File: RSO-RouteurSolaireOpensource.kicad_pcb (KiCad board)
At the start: 2 copper layers, 100 x 105 mm, 40 parts

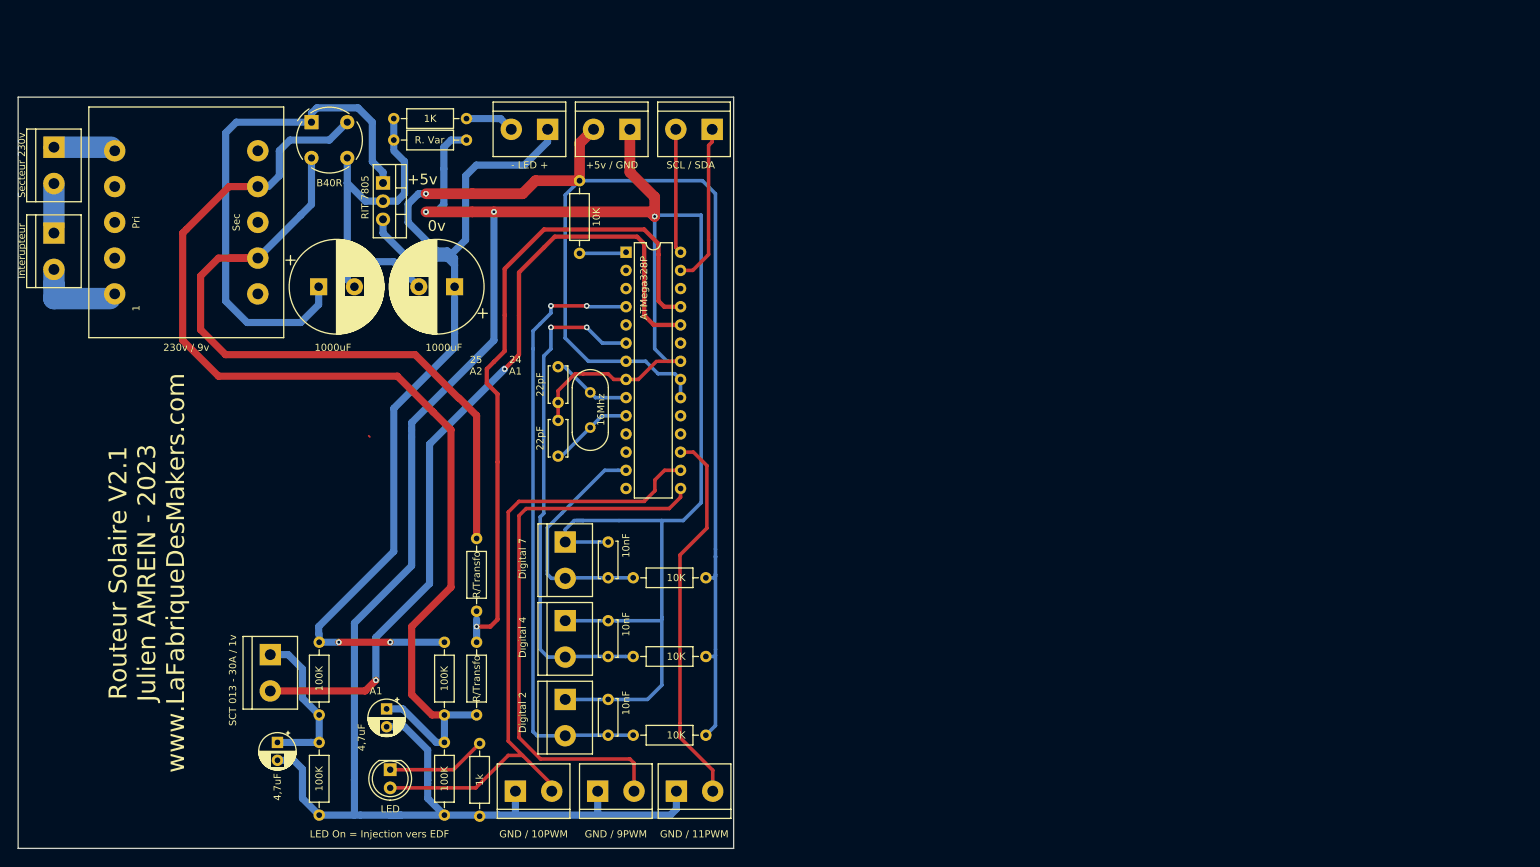
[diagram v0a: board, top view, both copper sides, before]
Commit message: MAJ Sur carte sct013
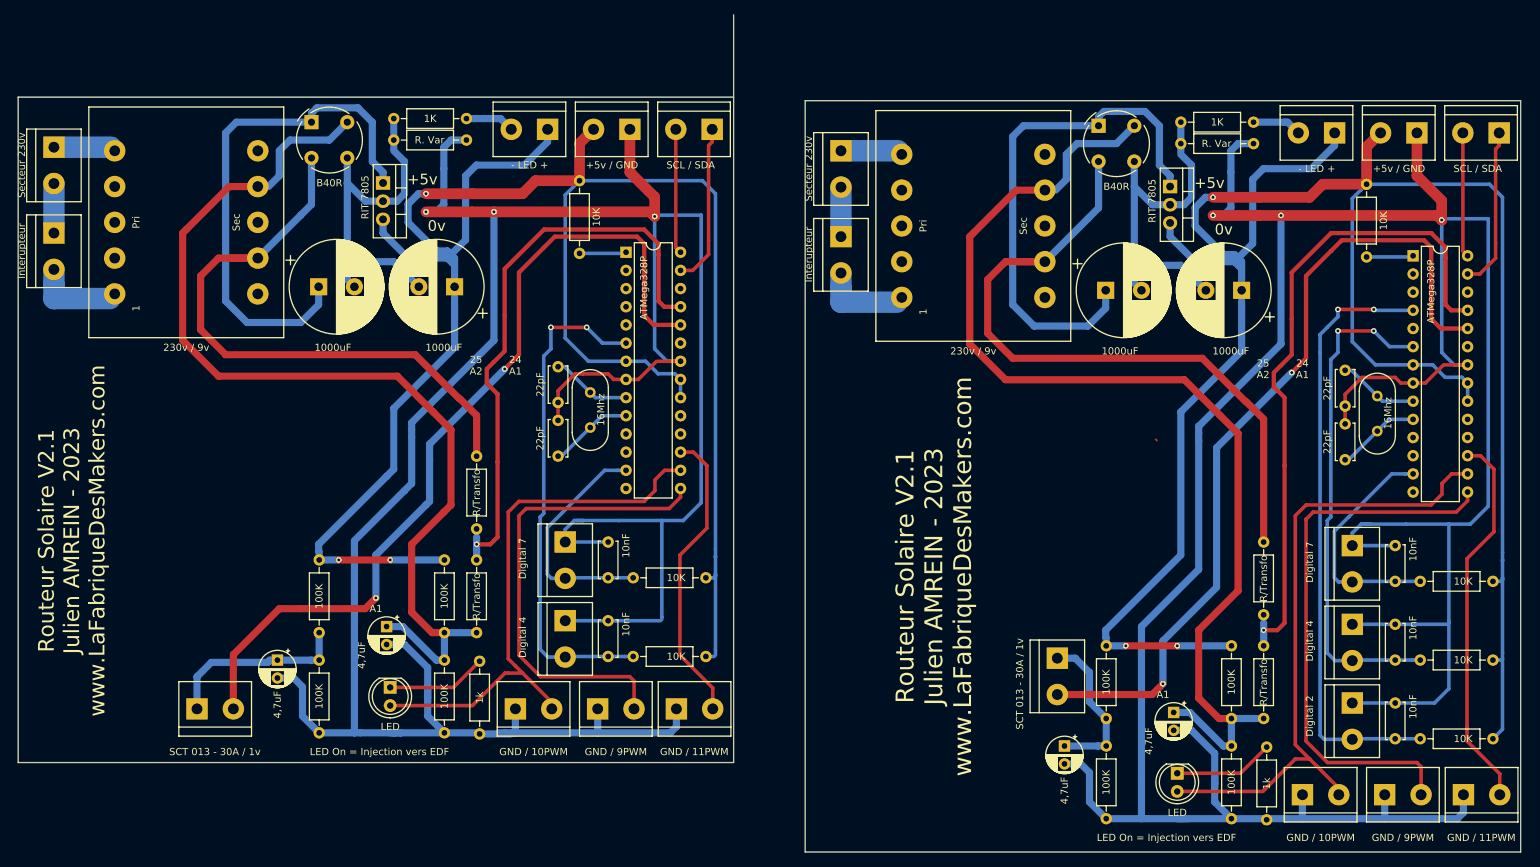
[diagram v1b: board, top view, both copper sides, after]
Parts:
- removed the 10K at (121.0, 143.7)
- removed the 10nF at (117.5, 138.7)
- removed the R/Transfo at (99.1, 116.2)
- removed the R/Transfo at (99.1, 130.7)
- removed the SCT 013 - 30A / 1v at (70.2, 132.4)
- added +5v / GND: TerminalBlock_bornier-2_P5.08mm, TerminalBlock:TerminalBlock_bornier-2_P5.08mm, F.Cu at (230.5, 59.5)
- added - LED +: TerminalBlock_bornier-2_P5.08mm, TerminalBlock:TerminalBlock_bornier-2_P5.08mm, F.Cu at (219.0, 59.5)
- added 1000uF: CP_Radial_D13.0mm_P5.00mm, Capacitor_THT:CP_Radial_D13.0mm_P5.00mm, F.Cu at (206.0, 81.5)
- added 1000uF: CP_Radial_D13.0mm_P5.00mm, Capacitor_THT:CP_Radial_D13.0mm_P5.00mm, F.Cu at (187.0, 81.5)
- added 100K: R_Axial_DIN0207_L6.3mm_D2.5mm_P10.16mm_Horizontal, Resistor_THT:R_Axial_DIN0207_L6.3mm_D2.5mm_P10.16mm_Horizontal, F.Cu at (204.6, 131.2)
- added 100K: R_Axial_DIN0207_L6.3mm_D2.5mm_P10.16mm_Horizontal, Resistor_THT:R_Axial_DIN0207_L6.3mm_D2.5mm_P10.16mm_Horizontal, F.Cu at (204.6, 145.2)
- added 100K: R_Axial_DIN0207_L6.3mm_D2.5mm_P10.16mm_Horizontal, Resistor_THT:R_Axial_DIN0207_L6.3mm_D2.5mm_P10.16mm_Horizontal, F.Cu at (187.1, 131.2)
- added 100K: R_Axial_DIN0207_L6.3mm_D2.5mm_P10.16mm_Horizontal, Resistor_THT:R_Axial_DIN0207_L6.3mm_D2.5mm_P10.16mm_Horizontal, F.Cu at (187.1, 145.2)
- added 10K: R_Axial_DIN0207_L6.3mm_D2.5mm_P10.16mm_Horizontal, Resistor_THT:R_Axial_DIN0207_L6.3mm_D2.5mm_P10.16mm_Horizontal, F.Cu at (223.5, 66.7)
- added 10K: R_Axial_DIN0207_L6.3mm_D2.5mm_P10.16mm_Horizontal, Resistor_THT:R_Axial_DIN0207_L6.3mm_D2.5mm_P10.16mm_Horizontal, F.Cu at (231.0, 133.2)
- added 10K: R_Axial_DIN0207_L6.3mm_D2.5mm_P10.16mm_Horizontal, Resistor_THT:R_Axial_DIN0207_L6.3mm_D2.5mm_P10.16mm_Horizontal, F.Cu at (231.0, 122.2)
- added 10K: R_Axial_DIN0207_L6.3mm_D2.5mm_P10.16mm_Horizontal, Resistor_THT:R_Axial_DIN0207_L6.3mm_D2.5mm_P10.16mm_Horizontal, F.Cu at (231.0, 144.2)
- added 10nF: C_Disc_D5.0mm_W2.5mm_P5.00mm, Capacitor_THT:C_Disc_D5.0mm_W2.5mm_P5.00mm, F.Cu at (227.5, 117.2)
- added 10nF: C_Disc_D5.0mm_W2.5mm_P5.00mm, Capacitor_THT:C_Disc_D5.0mm_W2.5mm_P5.00mm, F.Cu at (227.5, 128.2)
- added 10nF: C_Disc_D5.0mm_W2.5mm_P5.00mm, Capacitor_THT:C_Disc_D5.0mm_W2.5mm_P5.00mm, F.Cu at (227.5, 139.2)
- added 16Mhz: Crystal_HC18-U_Vertical, Crystal:Crystal_HC18-U_Vertical, F.Cu at (225.0, 101.2)
- added 1K: R_Axial_DIN0207_L6.3mm_D2.5mm_P10.16mm_Horizontal, Resistor_THT:R_Axial_DIN0207_L6.3mm_D2.5mm_P10.16mm_Horizontal, F.Cu at (197.5, 58.0)
- added 1k: R_Axial_DIN0207_L6.3mm_D2.5mm_P10.16mm_Horizontal, Resistor_THT:R_Axial_DIN0207_L6.3mm_D2.5mm_P10.16mm_Horizontal, F.Cu at (209.5, 155.5)
- added 22pF: C_Disc_D5.0mm_W2.5mm_P5.00mm, Capacitor_THT:C_Disc_D5.0mm_W2.5mm_P5.00mm, F.Cu at (220.5, 92.7)
- added 22pF: C_Disc_D5.0mm_W2.5mm_P5.00mm, Capacitor_THT:C_Disc_D5.0mm_W2.5mm_P5.00mm, F.Cu at (220.5, 100.2)
- added 230v / 9v: 230v - 5v AC, Transformer_THT:Transformer_CHK_EI30-2VA_1xSec, F.Cu at (158.5, 82.5)
- added 4,7uF: CP_Radial_D5.0mm_P2.50mm, Capacitor_THT:CP_Radial_D5.0mm_P2.50mm, F.Cu at (196.5, 140.5)
- added 4,7uF: CP_Radial_D5.0mm_P2.50mm, Capacitor_THT:CP_Radial_D5.0mm_P2.50mm, F.Cu at (181.2, 145.2)
- added ATMega328P: DIP-28_W7.62mm, Package_DIP:DIP-28_W7.62mm, F.Cu at (230.0, 76.7)
- added B40R: Diode_Bridge_Round_D9.0mm, Diode_THT:Diode_Bridge_Round_D9.0mm, F.Cu at (186.0, 58.5)
- added Digital 4: TerminalBlock_bornier-2_P5.08mm, TerminalBlock:TerminalBlock_bornier-2_P5.08mm, F.Cu at (221.5, 128.2)
- added Digital 7: TerminalBlock_bornier-2_P5.08mm, TerminalBlock:TerminalBlock_bornier-2_P5.08mm, F.Cu at (221.5, 117.2)
- added GND / 10PWM: TerminalBlock_bornier-2_P5.08mm, TerminalBlock:TerminalBlock_bornier-2_P5.08mm, F.Cu at (214.5, 152.0)
- added GND / 11PWM: TerminalBlock_bornier-2_P5.08mm, TerminalBlock:TerminalBlock_bornier-2_P5.08mm, F.Cu at (237.0, 152.0)
- added GND / 9PWM: TerminalBlock_bornier-2_P5.08mm, TerminalBlock:TerminalBlock_bornier-2_P5.08mm, F.Cu at (226.0, 152.0)
- added Interupteur: TerminalBlock_bornier-2_P5.08mm, TerminalBlock:TerminalBlock_bornier-2_P5.08mm, F.Cu at (150.0, 74.0)
- added LED: LED_D5.0mm, LED_THT:LED_D5.0mm, F.Cu at (197.0, 149.0)
- added R. Var: R_Axial_DIN0207_L6.3mm_D2.5mm_P10.16mm_Horizontal, Resistor_THT:R_Axial_DIN0207_L6.3mm_D2.5mm_P10.16mm_Horizontal, F.Cu at (197.5, 61.0)
- added R/Transfo: R_Axial_DIN0207_L6.3mm_D2.5mm_P10.16mm_Horizontal, Resistor_THT:R_Axial_DIN0207_L6.3mm_D2.5mm_P10.16mm_Horizontal, F.Cu at (209.1, 131.2)
- added R/Transfo: R_Axial_DIN0207_L6.3mm_D2.5mm_P10.16mm_Horizontal, Resistor_THT:R_Axial_DIN0207_L6.3mm_D2.5mm_P10.16mm_Horizontal, F.Cu at (209.1, 116.7)
- added R/Transfo: R_Axial_DIN0207_L6.3mm_D2.5mm_P10.16mm_Horizontal, Resistor_THT:R_Axial_DIN0207_L6.3mm_D2.5mm_P10.16mm_Horizontal, F.Cu at (99.1, 104.7)
- added R/Transfo: R_Axial_DIN0207_L6.3mm_D2.5mm_P10.16mm_Horizontal, Resistor_THT:R_Axial_DIN0207_L6.3mm_D2.5mm_P10.16mm_Horizontal, F.Cu at (99.1, 119.2)
- added RIT 7805: TO-220-3_Vertical, Package_TO_SOT_THT:TO-220-3_Vertical, F.Cu at (196.0, 67.0)
- added SCL / SDA: TerminalBlock_bornier-2_P5.08mm, TerminalBlock:TerminalBlock_bornier-2_P5.08mm, F.Cu at (242.0, 59.5)
- added SCT 013 - 30A / 1v: TerminalBlock_bornier-2_P5.08mm, TerminalBlock:TerminalBlock_bornier-2_P5.08mm, F.Cu at (60.0, 140.0)
- added SCT 013 - 30A / 1v: TerminalBlock_bornier-2_P5.08mm, TerminalBlock:TerminalBlock_bornier-2_P5.08mm, F.Cu at (180.2, 132.9)
- added Secteur 230v : TerminalBlock_bornier-2_P5.08mm, TerminalBlock:TerminalBlock_bornier-2_P5.08mm, F.Cu at (150.0, 62.0)
- moved Digital 2 110.0 mm to (221.5, 139.2)
- moved 100K 11.5 mm to (94.6, 119.2)
- moved 100K 11.5 mm to (77.1, 119.2)
- moved 100K 11.5 mm to (94.6, 133.2)
- moved 100K 11.5 mm to (77.1, 133.2)
- moved 1k 11.5 mm to (99.5, 143.5)
- moved 4,7uF 11.5 mm to (86.5, 128.5)
- moved 4,7uF 11.5 mm to (71.2, 133.2)
- moved GND / 10PWM 11.5 mm to (104.5, 140.0)
- moved GND / 11PWM 11.5 mm to (127.0, 140.0)
- moved GND / 9PWM 11.5 mm to (116.0, 140.0)
- moved LED 11.5 mm to (87.0, 137.0)
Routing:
- net (no net): track 1866.9 -> 3531.5 mm, vias 13 -> 24
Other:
- board size 100 x 105 mm -> 210 x 117 mm

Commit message: Gerber inclus
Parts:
- removed the +5v / GND at (230.5, 59.5)
- removed the - LED + at (219.0, 59.5)
- removed the 1000uF at (206.0, 81.5)
- removed the 1000uF at (187.0, 81.5)
- removed the 100K at (204.6, 131.2)
- removed the 100K at (204.6, 145.2)
- removed the 100K at (187.1, 131.2)
- removed the 100K at (187.1, 145.2)
- removed the 10K at (223.5, 66.7)
- removed the 10K at (231.0, 133.2)
- removed the 10K at (231.0, 122.2)
- removed the 10K at (231.0, 144.2)
- removed the 10K at (121.0, 132.7)
- removed the 10nF at (227.5, 117.2)
- removed the 10nF at (227.5, 128.2)
- removed the 10nF at (227.5, 139.2)
- removed the 10nF at (117.5, 127.7)
- removed the 16Mhz at (225.0, 101.2)
- removed the 1K at (197.5, 58.0)
- removed the 1k at (209.5, 155.5)
- removed the 22pF at (220.5, 92.7)
- removed the 22pF at (220.5, 100.2)
- removed the 230v / 9v at (158.5, 82.5)
- removed the 4,7uF at (196.5, 140.5)
- removed the 4,7uF at (181.2, 145.2)
- removed the ATMega328P at (230.0, 76.7)
- removed the B40R at (186.0, 58.5)
- removed Digital 2: TerminalBlock_bornier-2_P5.08mm, TerminalBlock:TerminalBlock_bornier-2_P5.08mm
- removed Digital 4: TerminalBlock_bornier-2_P5.08mm, TerminalBlock:TerminalBlock_bornier-2_P5.08mm (x2)
- removed the Digital 7 at (221.5, 117.2)
- removed the GND / 10PWM at (214.5, 152.0)
- removed the GND / 11PWM at (237.0, 152.0)
- removed the GND / 9PWM at (226.0, 152.0)
- removed the Interupteur at (150.0, 74.0)
- removed the LED at (197.0, 149.0)
- removed the R. Var at (197.5, 61.0)
- removed the R/Transfo at (209.1, 131.2)
- removed the R/Transfo at (209.1, 116.7)
- removed the R/Transfo at (99.1, 104.7)
- removed the R/Transfo at (99.1, 119.2)
- removed the RIT 7805 at (196.0, 67.0)
- removed the SCL / SDA at (242.0, 59.5)
- removed the SCT 013 - 30A / 1v at (180.2, 132.9)
- removed the Secteur 230v  at (150.0, 62.0)
- added ?: MountingHole_5mm, MountingHole:MountingHole_5mm, F.Cu at (40.5, 100.5)
- added ?: MountingHole_5mm, MountingHole:MountingHole_5mm, F.Cu at (78.0, 100.5)
- added ?: MountingHole_5mm, MountingHole:MountingHole_5mm, F.Cu at (129.5, 51.0)
- added ?: MountingHole_5mm, MountingHole:MountingHole_5mm, F.Cu at (129.5, 140.5)
- added ?: MountingHole_5mm, MountingHole:MountingHole_5mm, F.Cu at (40.5, 140.5)
- added ?: MountingHole_5mm, MountingHole:MountingHole_5mm, F.Cu at (40.5, 51.0)
- added R/Transfo: R_Axial_DIN0207_L6.3mm_D2.5mm_P10.16mm_Horizontal, Resistor_THT:R_Axial_DIN0207_L6.3mm_D2.5mm_P10.16mm_Horizontal, F.Cu at (99.1, 99.7)
- added R/Transfo: R_Axial_DIN0207_L6.3mm_D2.5mm_P10.16mm_Horizontal, Resistor_THT:R_Axial_DIN0207_L6.3mm_D2.5mm_P10.16mm_Horizontal, F.Cu at (99.1, 114.2)
- moved GND / 10PWM 11.0 mm to (104.5, 129.0)
- moved GND / 11PWM 11.0 mm to (127.0, 129.0)
- moved GND / 9PWM 11.0 mm to (116.0, 129.0)
- moved 4,7uF 8.28 mm to (72.5, 125.0)
- moved SCT 013 - 30A / 1v 7.13 mm to (65.1, 135.0)
- moved 100K 5.00 mm to (94.6, 128.2)
- moved 100K 5.00 mm to (94.6, 114.2)
- moved 100K 5.00 mm to (77.1, 128.2)
- moved 100K 5.00 mm to (77.1, 114.2)
- moved 1k 5.00 mm to (99.5, 138.5)
- moved 4,7uF 5.00 mm to (86.5, 123.5)
- moved LED 5.00 mm to (87.0, 132.0)
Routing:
- net (no net): track 3531.5 -> 1501.0 mm, vias 24 -> 9
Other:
- board size 210 x 117 mm -> 100 x 100.5 mm
- board text added: "Routeur Solaire Opensource GNU General Public License v3.0 www.LaFabriqueDesMakers.com Julien AMREIN - 2023 v2.2"
- board text removed: "LED On = Injection vers EDF"
- board text removed: "Routeur Solaire V2.1 Julien AMREIN - 2023 www.LaFabriqueDesMakers.com"
